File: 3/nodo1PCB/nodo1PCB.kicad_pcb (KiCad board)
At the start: 2 copper layers, 100 x 60 mm, 18 parts, among them J2 I2C, J3 Analog, J6 Analog, J7 Digital, K1 G3MB-202P

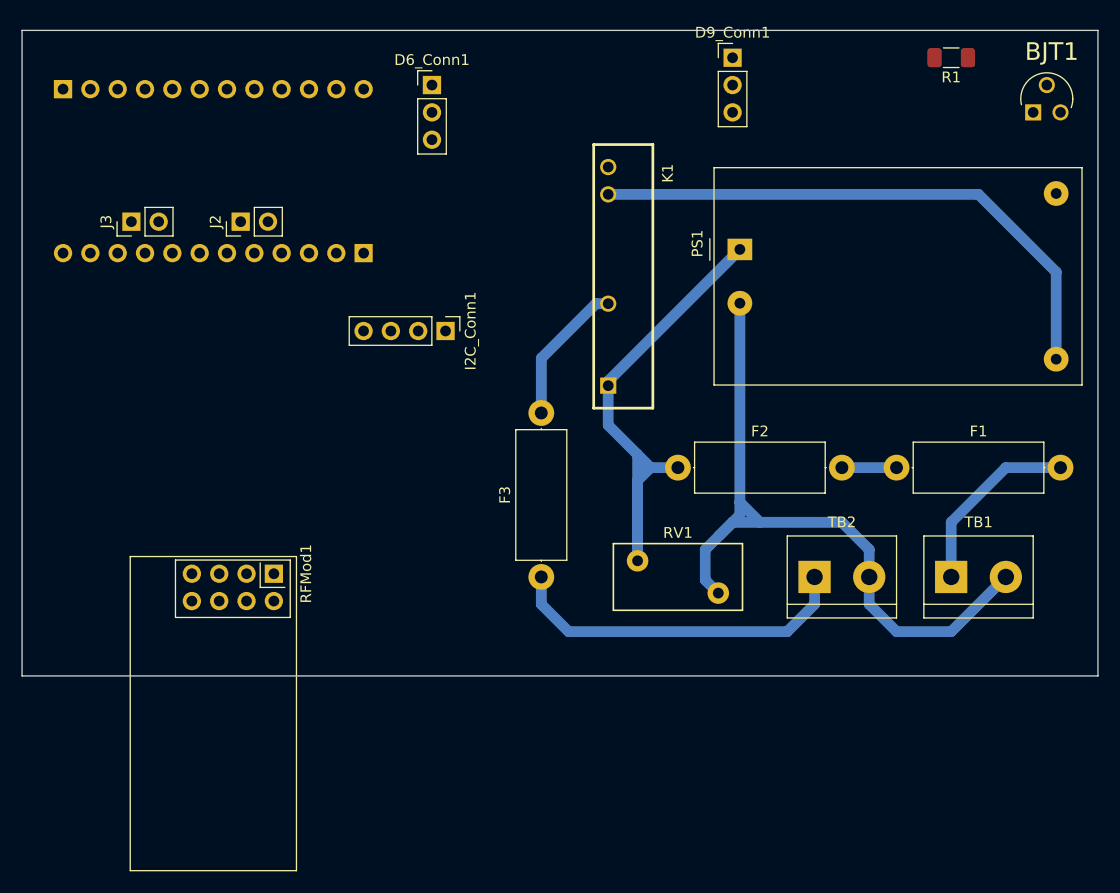
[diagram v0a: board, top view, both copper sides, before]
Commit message: Acabar layout alimentación PCB
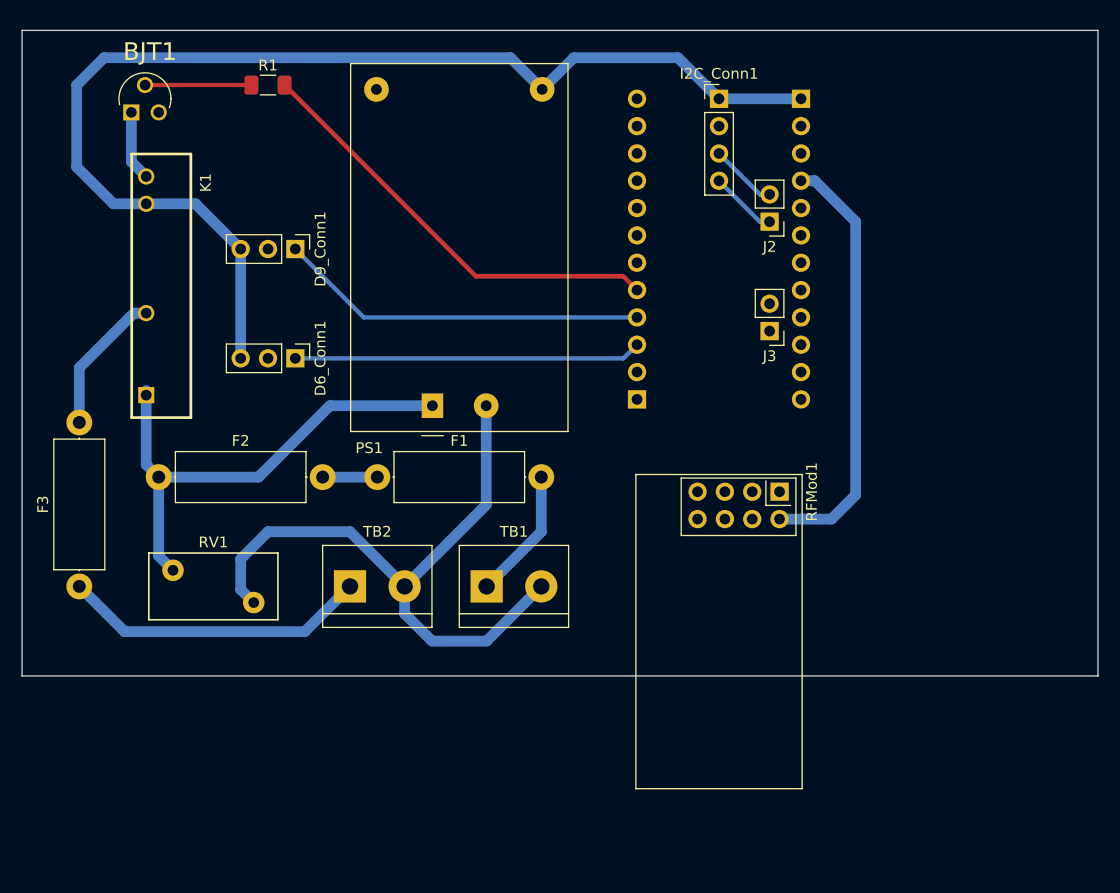
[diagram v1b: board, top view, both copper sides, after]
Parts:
- moved BJT1 83.8 mm to (51.7, 61.9)
- moved R1 63.6 mm to (61.9, 61.9), turned to 0 degrees
- moved J7 60.6 mm to (96.2, 91.1), turned to 0 degrees
- moved J3 60.2 mm to (108.5, 84.8), turned to 180 degrees
- moved J2 49.2 mm to (108.5, 74.6), turned to 180 degrees
- moved F2 48.3 mm to (51.7, 98.3)
- moved F1 48.3 mm to (72.1, 98.3)
- moved RFMod1 47.6 mm to (109.4, 99.7)
- moved D9_Conn1 44.4 mm to (64.4, 77.1), turned to -90 degrees
- moved TB1 43.2 mm to (82.2, 108.5)
- moved TB2 43.2 mm to (69.5, 108.5)
- moved RV1 43.2 mm to (60.6, 110.0)
- moved J6 43.1 mm to (111.4, 63.2), turned to 180 degrees
- moved F3 42.9 mm to (44.4, 108.5)
- moved K1 42.9 mm to (52.0, 80.6)
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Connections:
- D6_Conn1 pad 1: +5V -> /D7
- D6_Conn1 pad 3: /D7 -> +5V
- D9_Conn1 pad 1: +5V -> /*D6
- D9_Conn1 pad 3: /*D6 -> +5V
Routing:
- net +5V: track 52.7 -> 108.6 mm
- net /*D5: track 0.00 -> 40.6 mm
- net +3.3V: track 0.00 -> 40.1 mm
- net /*D6: track 0.00 -> 34.4 mm
- net /D7: track 0.00 -> 32.3 mm
- net Net-(BJT1-Pad2): track 0.00 -> 9.88 mm
- net Net-(PS1-Pad2): track 67.9 -> 61.3 mm
- net Net-(BJT1-Pad1): track 0.00 -> 6.53 mm
- net /SDA/A4: track 0.00 -> 6.28 mm
- net /SCL/A5: track 0.00 -> 6.28 mm
- net Net-(F1-Pad2): track 17.3 -> 12.3 mm
- net Net-(F3-Pad1): track 32.6 -> 28.6 mm
- net Net-(F2-Pad1): track 48.6 -> 45.9 mm

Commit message: Terminar PCB
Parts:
- removed J3: Analog, Connector_PinHeader_2.54mm:PinHeader_1x02_P2.54mm_Vertical
- added REF01: MountingHole_3mm, MountingHole:MountingHole_3mm, F.Cu at (42.9, 60.4)
- added REF02: MountingHole_3mm, MountingHole:MountingHole_3mm, F.Cu at (125.4, 60.4)
- added REF03: MountingHole_3mm, MountingHole:MountingHole_3mm, F.Cu at (42.9, 113.2)
- added REF04: MountingHole_3mm, MountingHole:MountingHole_3mm, F.Cu at (125.4, 113.2)
- R1: moved to B.Cu
- moved I2C_Conn1 16.5 mm to (120.3, 63.2)
- moved RFMod1 3.59 mm to (112.0, 97.2)
- moved D6_Conn1 2.54 mm to (67.0, 87.3)
- moved D9_Conn1 2.54 mm to (67.0, 77.1)
- moved J6 2.54 mm to (114.0, 63.2)
- moved TB1 2.54 mm to (84.8, 108.5)
- moved TB2 2.54 mm to (72.1, 108.5)
- moved BJT1 2.54 mm to (54.3, 61.9)
- moved F2 2.54 mm to (54.3, 98.3)
- moved F3 2.54 mm to (46.9, 108.5)
- moved K1 2.54 mm to (54.5, 80.6)
- moved R1 2.54 mm to (64.4, 61.9)
- moved RV1 2.54 mm to (63.1, 110.0)
- moved F1 2.54 mm to (74.6, 98.3)
- moved J2 2.54 mm to (111.1, 74.6)
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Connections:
- J2 pad 1: /SDA/A4 -> /SCL/A5
- J2 pad 2: /SCL/A5 -> /SDA/A4
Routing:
- net /D2: track 0.00 -> 29.6 mm
- net /SCK/D13: track 0.00 -> 24.0 mm
- net /*D9: track 0.00 -> 22.4 mm
- net /MISO/D12: track 0.00 -> 15.1 mm
- net /MOSI/*D11: track 0.00 -> 14.1 mm
- net /SCL/A5: track 6.28 -> 18.6 mm
- net /SS/*D10: track 0.00 -> 10.5 mm
- net /*D5: track 40.6 -> 47.5 mm
- net +5V: track 108.6 -> 114.9 mm
- net /SDA/A4: track 6.28 -> 10.9 mm
- net +3.3V: track 40.1 -> 40.7 mm
- net GND: track 0.00 -> 0.56 mm
- added copper zone on B.Cu, net GND
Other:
- board size 100 x 60 mm -> 90 x 60 mm
- board text added: "A.D.M."
